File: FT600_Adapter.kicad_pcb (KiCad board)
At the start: 4 copper layers, 80 x 70 mm, 22 parts, among them J1 CX70M-24P1, J2 Conn_02x20_Odd_Even, U1 FT600Q-T, Y1 30MHz

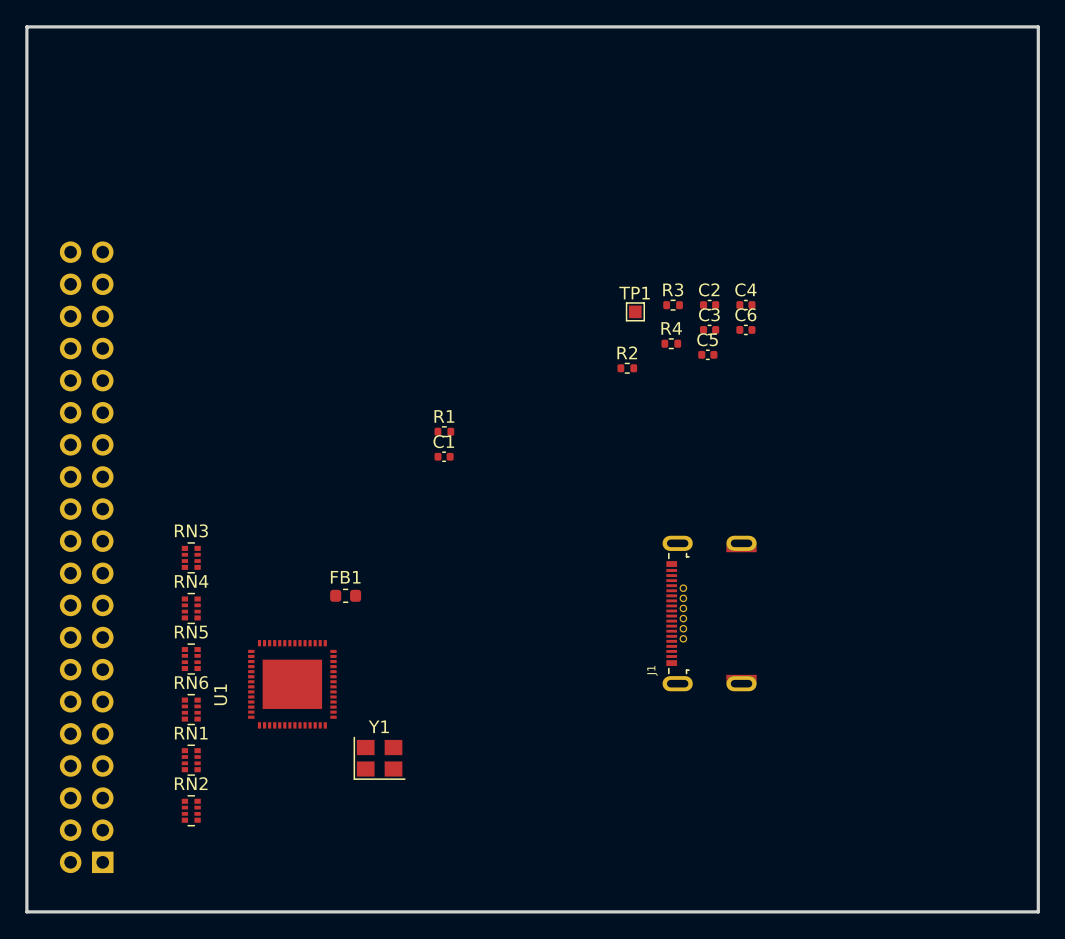
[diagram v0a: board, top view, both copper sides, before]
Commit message: Updated USB3.0 connector
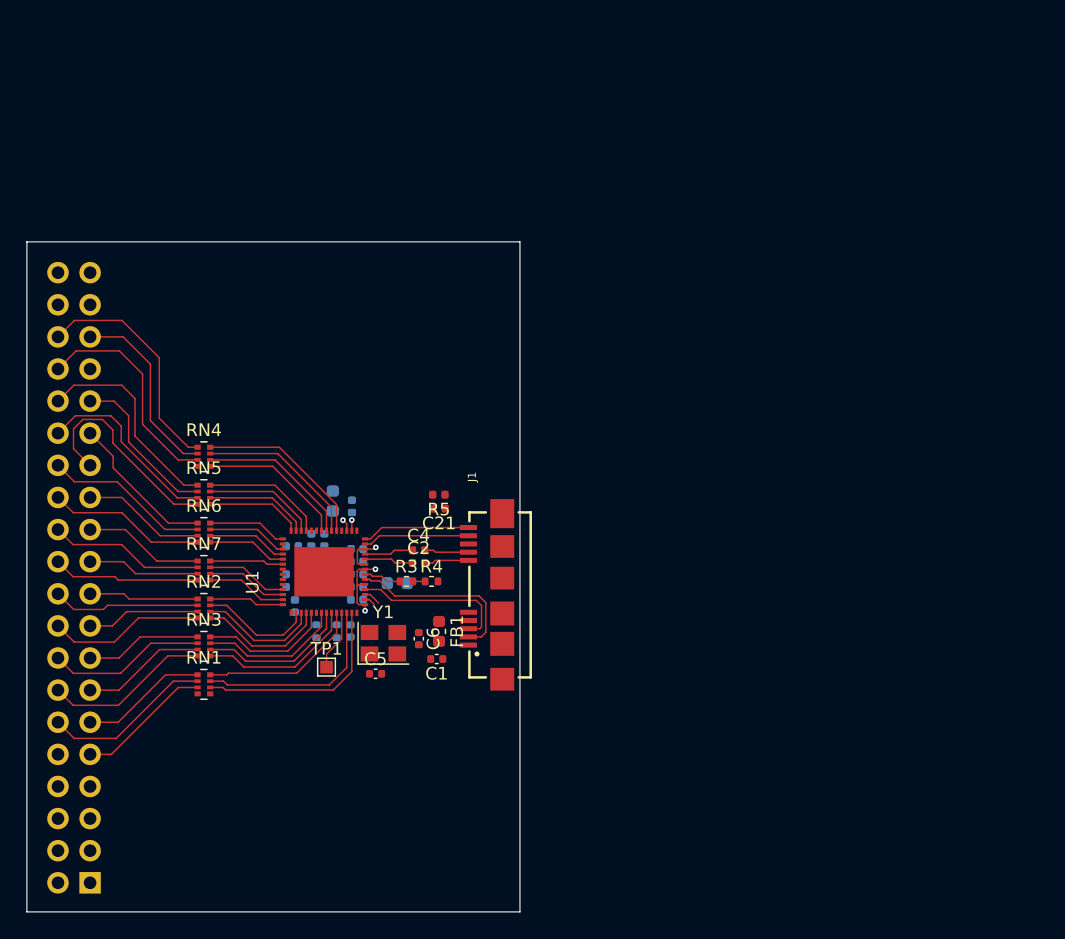
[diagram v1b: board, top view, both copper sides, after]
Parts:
- added C10: 100nF, Capacitor_SMD:C_0402_1005Metric, B.Cu at (121.0, 103.3)
- added C11: 100nF, Capacitor_SMD:C_0402_1005Metric, B.Cu at (123.5, 100.6)
- added C12: 100nF, Capacitor_SMD:C_0402_1005Metric, B.Cu at (121.2, 105.8)
- added C13: 4.7uF, Capacitor_SMD:C_0603_1608Metric, B.Cu at (129.3, 104.0)
- added C14: 100nF, Capacitor_SMD:C_0402_1005Metric, B.Cu at (126.1, 103.3)
- added C15: 100nF, Capacitor_SMD:C_0402_1005Metric, B.Cu at (126.1, 104.3)
- added C16: 100nF, Capacitor_SMD:C_0402_1005Metric, B.Cu at (126.1, 105.3)
- added C17: 100nF, Capacitor_SMD:C_0402_1005Metric, B.Cu at (121.0, 104.3)
- added C18: 100nF, Capacitor_SMD:C_0402_1005Metric, B.Cu at (121.0, 101.1)
- added C19: 100nF, Capacitor_SMD:C_0402_1005Metric, B.Cu at (122.5, 100.6)
- added C20: 100nF, Capacitor_SMD:C_0402_1005Metric, B.Cu at (125.7, 97.9)
- added C21: 100nF, Capacitor_SMD:C_0402_1005Metric, F.Cu at (132.6, 98.1)
- added C7: 4.7uF, Capacitor_SMD:C_0603_1608Metric, B.Cu at (124.2, 97.5)
- added C8: 100nF, Capacitor_SMD:C_0402_1005Metric, B.Cu at (126.1, 101.3)
- added C9: 100nF, Capacitor_SMD:C_0402_1005Metric, B.Cu at (126.1, 102.3)
- added R5: 1M, Resistor_SMD:R_0402_1005Metric, F.Cu at (132.6, 97.0)
- added RN7: 22R, Resistor_SMD:R_Array_Convex_4x0402, F.Cu at (114.0, 103.0)
- C3, R1, R2: moved to B.Cu
- J1: value CX70M-24P1 -> 692622030100; footprint footprint:HRS_CX70M-24P1 -> footprint:692622030100
- moved TP1 37.2 mm to (123.7, 110.6)
- moved C3 37.1 mm to (125.6, 107.8), turned to 270 degrees
- moved C5 36.4 mm to (127.6, 111.2)
- moved C6 35.6 mm to (131.0, 108.4), turned to 270 degrees
- moved C4 32.3 mm to (131.0, 101.4)
- moved R2 32.2 mm to (122.9, 107.8), turned to 90 degrees
- moved C2 30.8 mm to (131.0, 102.4)
- moved R3 30.4 mm to (130.0, 103.9)
- moved R4 26.7 mm to (132.0, 103.9)
- moved J1 19.0 mm to (137.6, 107.6)
- moved R1 17.9 mm to (124.5, 107.8), turned to 90 degrees
- moved RN2 16.0 mm to (114.0, 106.0)
- moved C1 16.0 mm to (132.4, 110.0), turned to 180 degrees
- moved RN6 14.0 mm to (114.0, 100.0)
- moved RN5 13.0 mm to (114.0, 97.0)
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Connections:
- net Net-(C2-Pad1) renamed /USB3_SSTX-
- net Net-(C4-Pad1) renamed /USB3_SSTX+
- net Net-(J2-Pad2) renamed +5V
- C2 pad 2: Net-(C2-Pad2) -> /USB3_SSTX_C-
- C3 pad 1: RESET_N -> /FTDI_RESETN
- C4 pad 2: Net-(C4-Pad2) -> /USB3_SSTX_C+
- J1 pad S6: Net-(J1-PadS6) -> /SHIELD
- J2 pad 1: Net-(J2-Pad1) -> GND
- J2 pad 11: Net-(J2-Pad11) -> /FPGA_RESETN
- J2 pad 12: Net-(J2-Pad12) -> /FPGA_GPIO0
- J2 pad 13: Net-(J2-Pad13) -> /FPGA_RDN
- J2 pad 14: Net-(J2-Pad14) -> /FPGA_OEN
- J2 pad 15: Net-(J2-Pad15) -> /FPGA_RXFN
- J2 pad 16: Net-(J2-Pad16) -> /FPGA_WRN
- J2 pad 17: Net-(J2-Pad17) -> /FPGA_BE1
- J2 pad 18: Net-(J2-Pad18) -> /FPGA_TXEN
- J2 pad 19: Net-(J2-Pad19) -> /FPGA_D15
- J2 pad 20: Net-(J2-Pad20) -> /FPGA_BE0
- J2 pad 21: Net-(J2-Pad21) -> /FPGA_D13
- J2 pad 22: Net-(J2-Pad22) -> /FPGA_D14
- J2 pad 23: Net-(J2-Pad23) -> /FPGA_D11
- J2 pad 24: Net-(J2-Pad24) -> /FPGA_D12
- J2 pad 25: Net-(J2-Pad25) -> /FPGA_D9
- J2 pad 26: Net-(J2-Pad26) -> /FPGA_D10
- J2 pad 27: Net-(J2-Pad27) -> /FPGA_D7
- J2 pad 28: Net-(J2-Pad28) -> /FPGA_D8
- J2 pad 29: Net-(J2-Pad29) -> /FPGA_CLK
- J2 pad 30: Net-(J2-Pad30) -> /FPGA_D6
- J2 pad 31: Net-(J2-Pad31) -> /FPGA_D5
- J2 pad 32: Net-(J2-Pad32) -> /FPGA_D4
- J2 pad 33: Net-(J2-Pad33) -> /FPGA_D3
- J2 pad 34: Net-(J2-Pad34) -> /FPGA_D2
- J2 pad 35: Net-(J2-Pad35) -> /FPGA_D1
- J2 pad 36: Net-(J2-Pad36) -> /FPGA_D0
- J2 pad 37: Net-(J2-Pad37) -> GND
- J2 pad 38: Net-(J2-Pad38) -> GND
- J2 pad 39: Net-(J2-Pad39) -> +3V3
- J2 pad 40: Net-(J2-Pad40) -> +3V3
- J2 pad 9: Net-(J2-Pad9) -> /FPGA_GPIO1
- R1 pad 2: RESET_N -> /FTDI_RESETN
- RN1 pad 1: Net-(RN1-Pad1) -> /FPGA_RESETN
- RN1 pad 2: Net-(RN1-Pad2) -> /FPGA_GPIO0
- RN1 pad 3: Net-(RN1-Pad3) -> /FPGA_GPIO1
- RN1 pad 5: /FTDI_RXF_N -> Net-(RN1-Pad5)
- RN1 pad 6: /FTDI_TXE_N -> /FTDI_GPIO1
- RN1 pad 7: /FTDI_BE_1 -> /FTDI_GPIO0
- RN1 pad 8: /FTDI_BE_0 -> /FTDI_RESETN
- RN2 pad 1: Net-(RN2-Pad1) -> /FPGA_D15
- RN2 pad 2: Net-(RN2-Pad2) -> /FPGA_BE0
- RN2 pad 3: Net-(RN2-Pad3) -> /FPGA_BE1
- RN2 pad 4: Net-(RN2-Pad4) -> /FPGA_TXEN
- RN2 pad 5: Net-(RN2-Pad5) -> /FTDI_TXE_N
- RN2 pad 6: /FTDI_OE_N -> /FTDI_BE_1
- RN2 pad 7: /FTDI_RD_N -> /FTDI_BE_0
- RN2 pad 8: /FTDI_WR_N -> /FTDI_DATA_15
- RN3 pad 1: Net-(RN3-Pad1) -> /FPGA_RXFN
- RN3 pad 2: Net-(RN3-Pad2) -> /FPGA_WRN
- RN3 pad 3: Net-(RN3-Pad3) -> /FPGA_RDN
- RN3 pad 4: Net-(RN3-Pad4) -> /FPGA_OEN
- RN3 pad 5: /FTDI_DATA_3 -> /FTDI_OE_N
- RN3 pad 6: /FTDI_DATA_2 -> /FTDI_RD_N
- RN3 pad 7: /FTDI_DATA_1 -> /FTDI_WR_N
- RN3 pad 8: /FTDI_DATA_0 -> /FTDI_RXF_N
- RN4 pad 1: Net-(RN4-Pad1) -> /FPGA_D0
- RN4 pad 2: Net-(RN4-Pad2) -> /FPGA_D1
- RN4 pad 3: Net-(RN4-Pad3) -> /FPGA_D2
- RN4 pad 4: Net-(RN4-Pad4) -> /FPGA_D3
- RN4 pad 5: /FTDI_DATA_7 -> /FTDI_DATA_3
- RN4 pad 6: /FTDI_DATA_6 -> /FTDI_DATA_2
- RN4 pad 7: /FTDI_DATA_5 -> /FTDI_DATA_1
- RN4 pad 8: /FTDI_DATA_4 -> /FTDI_DATA_0
- RN5 pad 1: Net-(RN5-Pad1) -> /FPGA_D4
- RN5 pad 2: Net-(RN5-Pad2) -> /FPGA_D5
- RN5 pad 3: Net-(RN5-Pad3) -> /FPGA_D6
- RN5 pad 4: Net-(RN5-Pad4) -> /FPGA_D7
- RN5 pad 5: /FTDI_DATA_11 -> /FTDI_DATA_7
- RN5 pad 6: /FTDI_DATA_10 -> /FTDI_DATA_6
- RN5 pad 7: /FTDI_DATA_9 -> /FTDI_DATA_5
- RN5 pad 8: /FTDI_DATA_8 -> /FTDI_DATA_4
- RN6 pad 1: Net-(RN6-Pad1) -> /FPGA_CLK
- RN6 pad 2: Net-(RN6-Pad2) -> /FPGA_D8
- RN6 pad 3: Net-(RN6-Pad3) -> /FPGA_D9
- RN6 pad 4: Net-(RN6-Pad4) -> /FPGA_D10
- RN6 pad 5: /FTDI_DATA_15 -> /FTDI_DATA_10
- RN6 pad 6: /FTDI_DATA_14 -> /FTDI_DATA_9
- RN6 pad 7: /FTDI_DATA_13 -> /FTDI_DATA_8
- RN6 pad 8: /FTDI_DATA_12 -> /FTDI_CLK
- U1 pad 1: Net-(U1-Pad1) -> +1V0
- U1 pad 10: RESET_N -> /FTDI_RESETN
- U1 pad 15: Net-(U1-Pad15) -> +3V3
- U1 pad 18: Net-(U1-Pad18) -> /USB2_D+
- U1 pad 19: Net-(U1-Pad19) -> +3V3
- U1 pad 20: Net-(U1-Pad20) -> /USB2_D-
- U1 pad 22: Net-(U1-Pad22) -> +3V3
- U1 pad 23: Net-(U1-Pad23) -> +1V0
- U1 pad 26: Net-(U1-Pad26) -> +1V0
- U1 pad 27: Net-(U1-Pad27) -> /USB3_SSRX-
- U1 pad 28: Net-(U1-Pad28) -> /USB3_SSRX+
- U1 pad 30: Net-(U1-Pad30) -> +3V3
- U1 pad 31: Net-(U1-Pad31) -> +1V0
- U1 pad 32: Net-(U1-Pad32) -> GND
- U1 pad 37: Net-(U1-Pad37) -> +1V0
- U1 pad 38: Net-(U1-Pad38) -> +3V3
- U1 pad 44: Net-(U1-Pad44) -> +3V3
- U1 pad 49: Net-(U1-Pad49) -> GND
- U1 pad 50: Net-(U1-Pad50) -> +1V0
- U1 pad 51: Net-(U1-Pad51) -> GND
- U1 pad 52: Net-(U1-Pad52) -> +3V3
- U1 pad 57: Net-(U1-Pad57) -> GND
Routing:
- net /FPGA_D0: track 0.00 -> 18.5 mm
- net /FPGA_D2: track 0.00 -> 17.5 mm
- net /FPGA_D7: track 0.00 -> 16.9 mm
- net /FPGA_D4: track 0.00 -> 16.6 mm
- net /FTDI_GPIO1: track 0.00 -> 16.5 mm
- net /FTDI_GPIO0: track 0.00 -> 15.8 mm
- net /FPGA_D6: track 0.00 -> 15.0 mm
- net /FPGA_D1: track 0.00 -> 14.9 mm
- net /USB2_D-: track 0.00 -> 14.2 mm
- net /FTDI_DATA_0: track 0.00 -> 13.9 mm
- net /FPGA_GPIO0: track 0.00 -> 13.4 mm
- net /FTDI_DATA_1: track 0.00 -> 13.2 mm
- net /FPGA_OEN: track 0.00 -> 13.2 mm
- net /FPGA_D8: track 0.00 -> 13.1 mm
- net /FTDI_RESETN: track 0.00 -> 13.0 mm
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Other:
- board size 80 x 70 mm -> 39 x 53 mm
- net class Default: clearance 0.2 -> 0.15; trace_width 0.25 -> 0.12; via_dia 0.8 -> 0.45; via_drill 0.4 -> 0.2
- net class GND added: clearance 0.15, trace_width 0.35, via_dia 0.45, via_drill 0.2
- net class PWR added: clearance 0.15, trace_width 0.25, via_dia 0.45, via_drill 0.2
- rule trace_clearance: 0.2 -> 0.15
- rule trace_min: 0.2 -> 0.08
- rule via_min_drill: 0.3 -> 0.2

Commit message: Updated PCB layout
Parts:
- added D1: GREEN, LED_SMD:LED_0603_1608Metric, F.Cu at (130.0, 114.2)
- added R6: 10K, Resistor_SMD:R_0402_1005Metric, F.Cu at (127.0, 114.2)
- added REF**: OSHW-Logo2_14.6x12mm_SilkScreen, Symbol:OSHW-Logo2_14.6x12mm_SilkScreen, F.Cu at (123.5, 86.7)
- TP1: moved to B.Cu
- moved RN1 11.8 mm to (125.2, 108.6), turned to 90 degrees
- moved RN4 10.7 mm to (124.0, 97.6), turned to 270 degrees
- moved RN3 8.56 mm to (122.5, 108.6), turned to 90 degrees
- moved RN5 7.37 mm to (121.3, 97.6), turned to 270 degrees
- moved J2 7.00 mm to (112.0, 127.7)
- moved RN2 6.40 mm to (119.8, 108.6), turned to 90 degrees
- moved RN6 4.35 mm to (118.1, 101.5)
- moved RN7 4.26 mm to (118.1, 104.2)
- moved TP1 3.85 mm to (121.2, 107.8)
- moved FB1 1.68 mm to (132.9, 109.5)
- moved C1 1.65 mm to (132.4, 111.7)
- moved C12 1.00 mm to (121.5, 104.8), turned to 0 degrees
- moved C6 0.74 mm to (131.6, 108.9)
- moved Y1 0.74 mm to (128.8, 109.2)
- moved C5 0.74 mm to (128.1, 111.7)
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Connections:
- net Net-(C1-Pad1) renamed /CONN_VBUS
- J1 pad S1: Net-(J1-PadS1) -> /SHIELD
- J1 pad S2: Net-(J1-PadS2) -> /SHIELD
- J1 pad S3: Net-(J1-PadS3) -> /SHIELD
- J1 pad S4: Net-(J1-PadS4) -> /SHIELD
- J1 pad S5: Net-(J1-PadS5) -> /SHIELD
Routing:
- net +3V3: track 6.71 -> 68.7 mm, vias 3 -> 6
- net +5V: track 0.00 -> 22.6 mm, vias 0 -> 1
- net /FPGA_D3: track 0.00 -> 22.6 mm
- net +1V0: track 4.17 -> 26.5 mm, vias 2 -> 4
- net GND: track 0.00 -> 18.0 mm, vias 0 -> 32
- net VBUS: track 0.00 -> 16.2 mm, vias 0 -> 3
- net /FTDI_GPIO1: track 16.5 -> 1.83 mm
- net /FTDI_GPIO0: track 15.8 -> 1.87 mm
- net /FPGA_D15: track 8.67 -> 22.5 mm
- net /FPGA_BE1: track 8.97 -> 22.6 mm
- net /FPGA_D13: track 8.89 -> 22.4 mm
- net /FPGA_RXFN: track 9.19 -> 22.6 mm
- net /FPGA_D11: track 9.53 -> 22.5 mm
- net /FPGA_D9: track 9.76 -> 22.5 mm
- net /FPGA_RDN: track 9.83 -> 22.5 mm
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- added copper zone on F.Cu, net /CONN_VBUS
- added copper zone on F.Cu, net /SHIELD
- added copper zone on B.Cu, net GND
- added copper zone on F.Cu, net GND
- added copper zone on In1.Cu, net GND
- added copper zone on In2.Cu, net GND
- added copper zone on F.Cu, net VBUS
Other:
- board size 39 x 53 mm -> 32 x 53 mm
- net class GND: trace_width 0.35 -> 0.25
- net class Outer_Impedance_50_90 added: clearance 0.15, trace_width 0.12, via_dia 0.45, via_drill 0.2
- board text added: "FT600 ADAPTER"

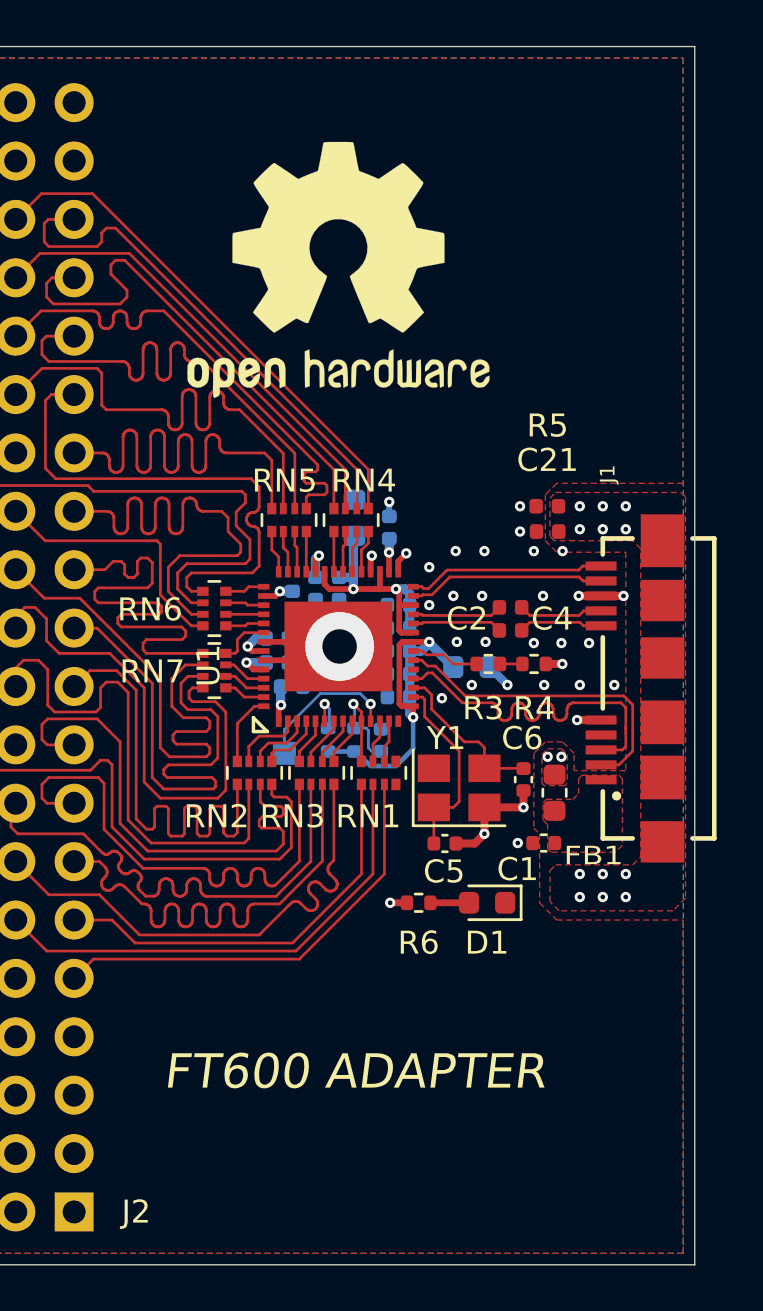
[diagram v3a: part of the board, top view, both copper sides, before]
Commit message: Added GND array vias, stand off through holes
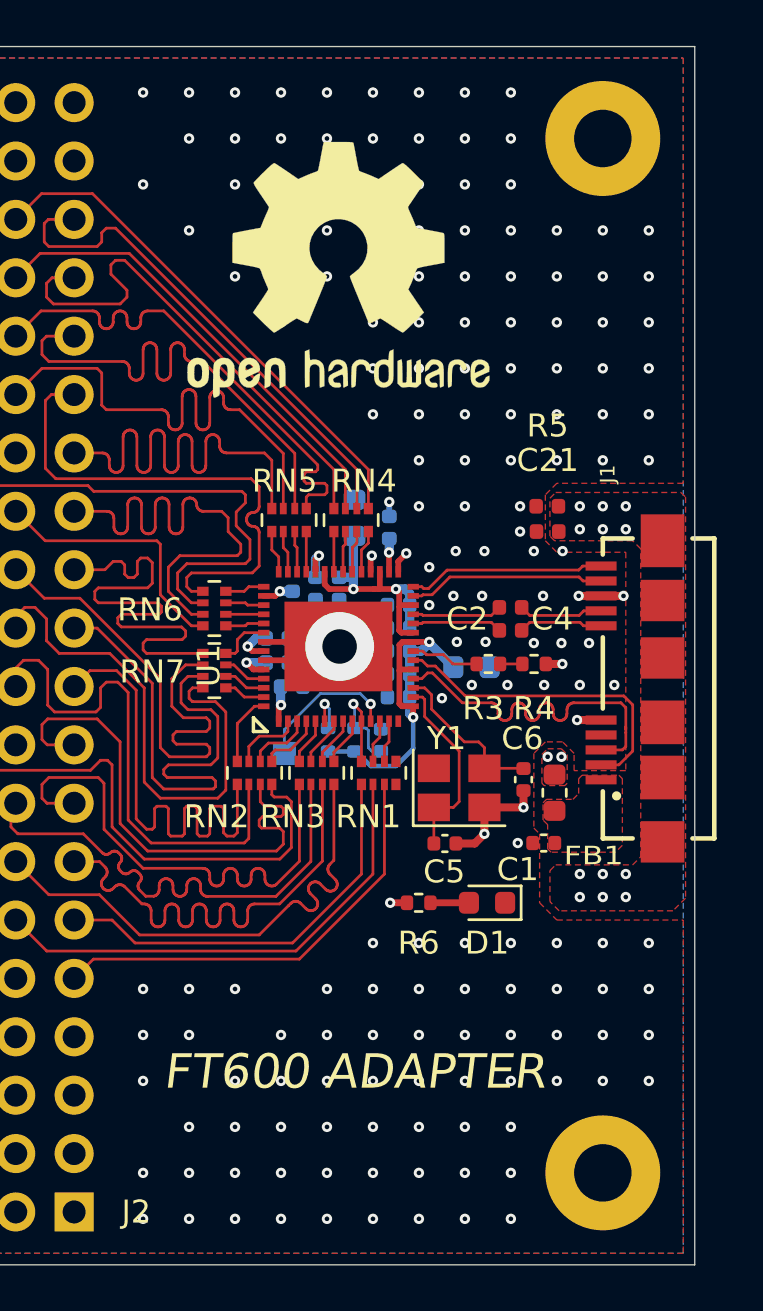
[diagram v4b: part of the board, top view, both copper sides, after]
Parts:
- added REF**: MountingHole_2.5mm_Pad, MountingHole:MountingHole_2.5mm_Pad, F.Cu at (135.0, 126.0)
- added REF**: MountingHole_2.5mm_Pad, MountingHole:MountingHole_2.5mm_Pad, F.Cu at (135.0, 81.0)
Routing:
- net GND: track 18.0 -> 16.9 mm, vias 32 -> 172
- net +3V3: track 68.7 -> 69.3 mm
